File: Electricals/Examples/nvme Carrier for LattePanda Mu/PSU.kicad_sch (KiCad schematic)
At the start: 176 parts, among them J17 Barrel_Jack_Switch, J79 Conn_01x02_Pin, J80 Conn_01x02_Pin, Q5 2N7002, Q6 2N7002, Q7 NCE30P28Q, Q8 2N7002, SW1 SW_Push, SW2 SW_Push, U13 TL431DBZ, U15 SY8253ADC, U16 SY8253ADC, U400 SY8253ADC, U410 SY8253ADC, U420 SY8253ADC, U430 SY8253ADC, U440 SY8253ADC, U450 SY8253ADC, U460 SY8253ADC, U470 SY8253ADC

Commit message: Some small changes
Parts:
- renumbered J17 to J5
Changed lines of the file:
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@@
 		(dnp no)
 		(fields_autoplaced yes)
-		(property "Reference" "J17"
+		(property "Reference" "J5"
 			(at 58.42 99.06 0)
 			(effects
@@
 			(project "nvme Carrier for LattePanda Mu"
 				(path "/2a6d114a-7fd7-4207-b5f7-4ea9c34f36aa/b23aee49-27d1-466d-98e2-113ee657e42b"
-					(reference "J17")
+					(reference "J5")
 					(unit 1)
 				)

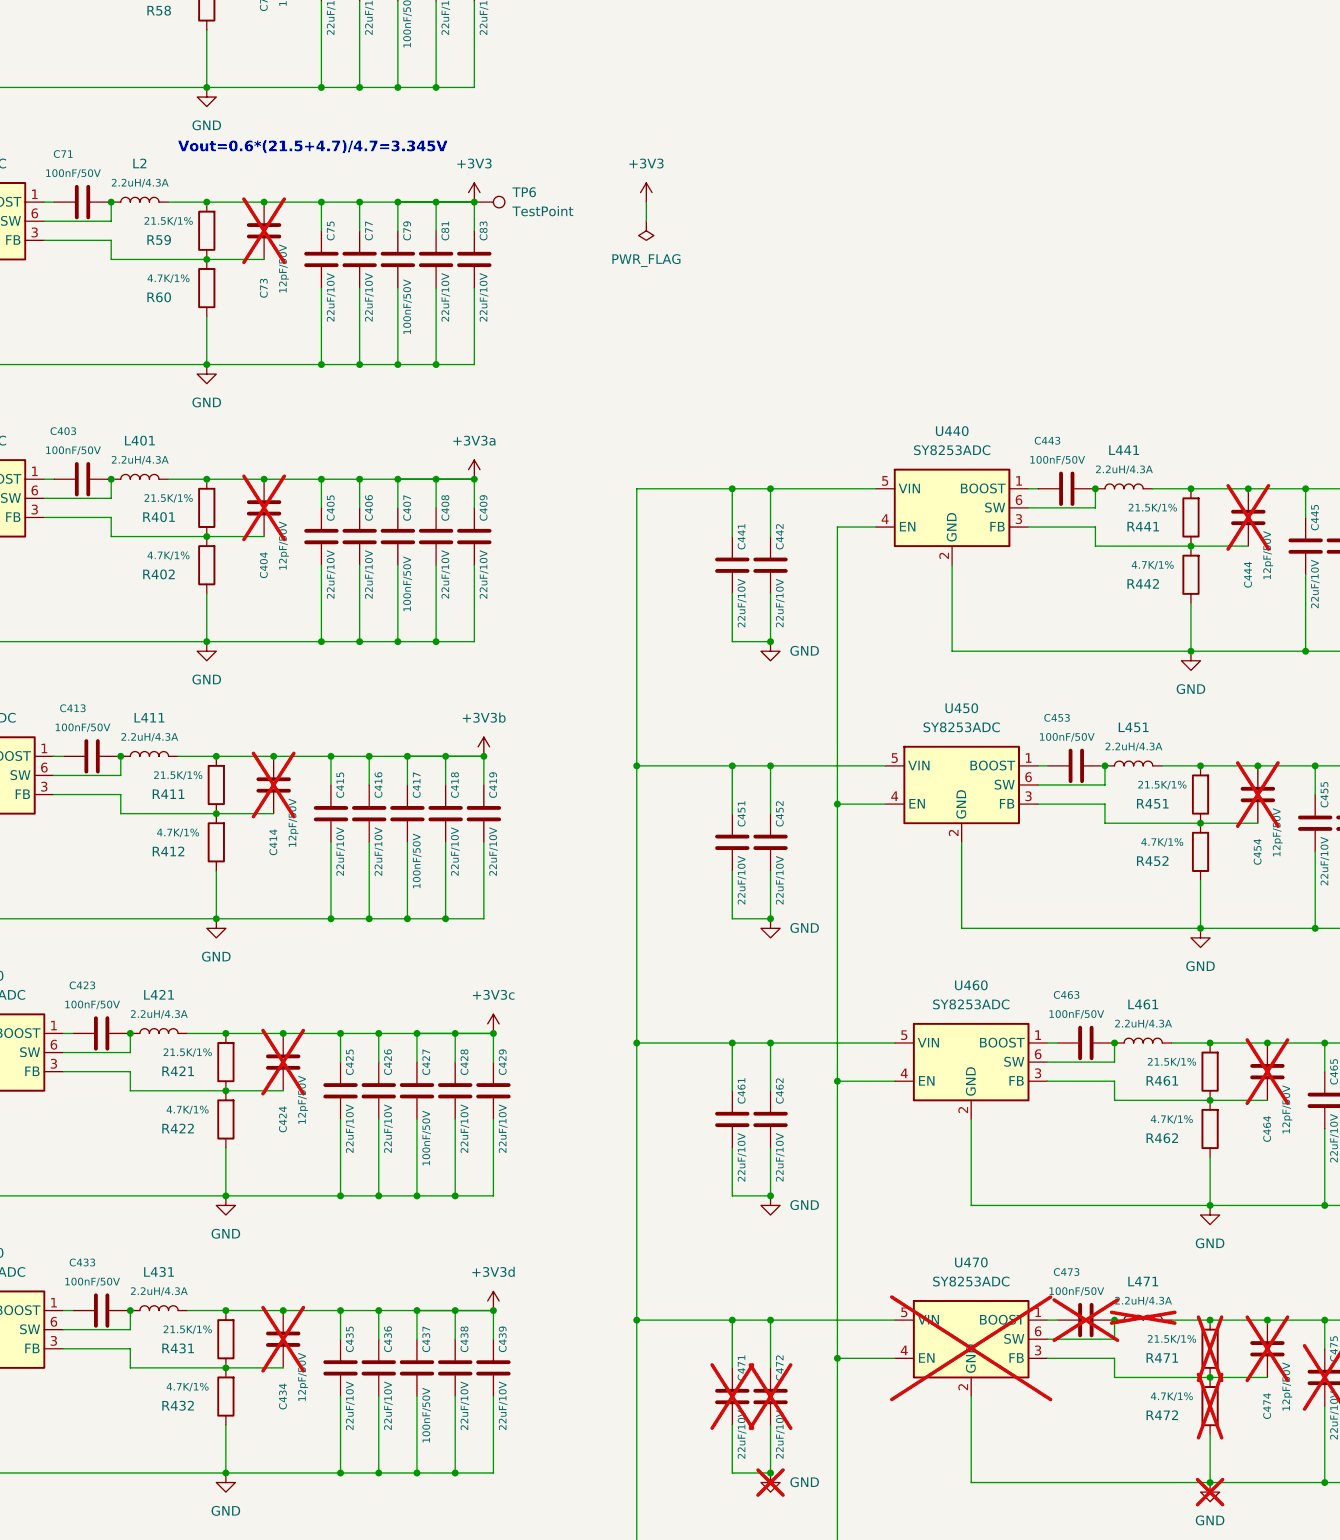
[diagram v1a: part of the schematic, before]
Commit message: Layout optimization + internal USB
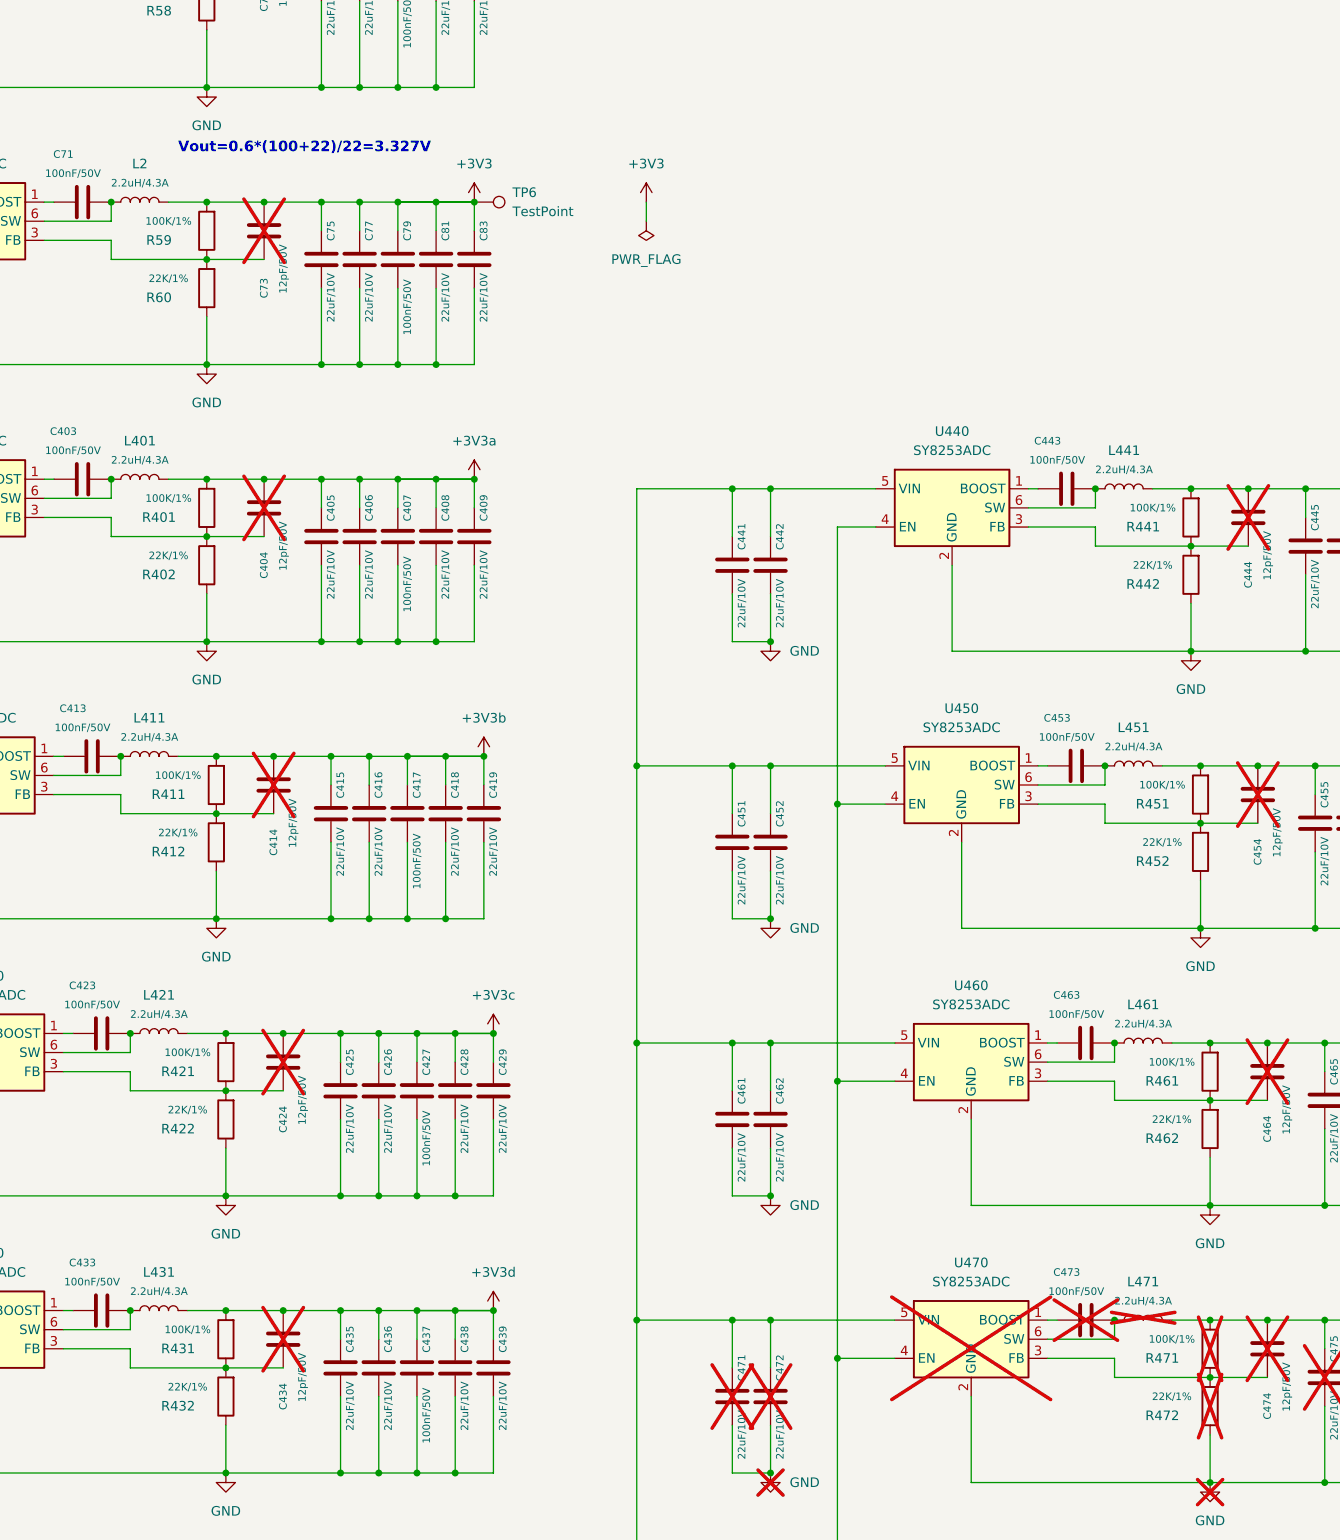
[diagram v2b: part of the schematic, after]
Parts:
- R401, R411, R421, R431, R441, R451, R461, R471, R59: value 21.5K/1% -> 100K/1%
- R402, R412, R422, R432, R442, R452, R462, R472, R60: value 4.7K/1% -> 22K/1%
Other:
- note added: "Vout=0.6*(100+22)/22=3.327V"
- note removed: "Vout=0.6*(21.5+4.7)/4.7=3.345V"
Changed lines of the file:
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@@
 		)
 	)
-	(text "Vout=0.6*(21.5+4.7)/4.7=3.345V"
+	(text "Vout=0.6*(100+22)/22=3.327V"
 		(exclude_from_sim no)
 		(at 353.06 137.16 0)
@@
 			)
 		)
-		(property "Value" "21.5K/1%"
+		(property "Value" "100K/1%"
 			(at 482.6 184.15 0)
 			(effects
@@
 			)
 		)
-		(property "Value" "21.5K/1%"
+		(property "Value" "100K/1%"
 			(at 354.33 256.54 0)
 			(effects
@@
 			)
 		)
-		(property "Value" "4.7K/1%"
+		(property "Value" "22K/1%"
 			(at 354.33 264.16 0)
 			(effects
@@
 			)
 		)
-		(property "Value" "4.7K/1%"
+		(property "Value" "22K/1%"
 			(at 483.87 228.6 0)
 			(effects
@@
 			)
 		)
-		(property "Value" "4.7K/1%"
+		(property "Value" "22K/1%"
 			(at 351.79 190.5 0)
 			(effects
@@
 			)
 		)
-		(property "Value" "4.7K/1%"
+		(property "Value" "22K/1%"
 			(at 351.79 153.67 0)
 			(effects
@@
 			)
 		)
-		(property "Value" "4.7K/1%"
+		(property "Value" "22K/1%"
 			(at 354.33 300.99 0)
 			(effects
@@
 			)
 		)
-		(property "Value" "21.5K/1%"
+		(property "Value" "100K/1%"
 			(at 353.06 219.71 0)
 			(effects
@@
 			)
 		)
-		(property "Value" "4.7K/1%"
+		(property "Value" "22K/1%"
 			(at 482.6 191.77 0)
 			(effects
@@
 			)
 		)
-		(property "Value" "4.7K/1%"
+		(property "Value" "22K/1%"
 			(at 485.14 265.43 0)
 			(effects
@@
 			)
 		)
-		(property "Value" "21.5K/1%"
+		(property "Value" "100K/1%"
 			(at 351.79 146.05 0)
 			(effects
@@
 			)
 		)
-		(property "Value" "4.7K/1%"
+		(property "Value" "22K/1%"
 			(at 485.14 302.26 0)
 			(effects
@@
 			)
 		)
-		(property "Value" "21.5K/1%"
+		(property "Value" "100K/1%"
 			(at 483.87 220.98 0)
 			(effects
@@
 			)
 		)
-		(property "Value" "21.5K/1%"
+		(property "Value" "100K/1%"
 			(at 351.79 182.88 0)
 			(effects
@@
 			)
 		)
-		(property "Value" "21.5K/1%"
+		(property "Value" "100K/1%"
 			(at 485.14 294.64 0)
 			(effects
@@
 			)
 		)
-		(property "Value" "21.5K/1%"
+		(property "Value" "100K/1%"
 			(at 354.33 293.37 0)
 			(effects
@@
 			)
 		)
-		(property "Value" "4.7K/1%"
+		(property "Value" "22K/1%"
 			(at 353.06 227.33 0)
 			(effects
@@
 			)
 		)
-		(property "Value" "21.5K/1%"
+		(property "Value" "100K/1%"
 			(at 485.14 257.81 0)
 			(effects
